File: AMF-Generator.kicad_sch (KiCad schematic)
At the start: 47 parts, among them Q1 ISC012N04LM6ATMA1, Q2 ISC012N04LM6ATMA1, T1 PL300-104L, U1 ACS732KLATR-75AB, U2 UCC21540

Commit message: Basically done with schematic, will split to different PCBs now
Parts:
- C10, C11, C12, C13, C14, C15, C16, C17, C18, C19, C20, C21, C4, C5, C6, C7, C8, C9: footprint (none) -> Capacitor_SMD:C_2220_5650Metric
- C34, C35, C36, C37: footprint (none) -> Capacitor_SMD:C_0805_2012Metric
- R1, R2, R3, R4, R5, R6, R7: footprint (none) -> Resistor_SMD:R_0805_2012Metric
- R10, R8: value 180m -> 1
- R11: value R_Small -> 3.3K
- R12: value R_Small -> 1K
- R9: value 510m -> 1
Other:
- note added: "Double check capacitor ampacity"
- note added: "TODOS: x Bypass Caps x Pullup R values? x Define R11, R12 x Rerun LTSPICE with new gate resistor order x Set I2C ADDR * Double check capacitor ampacity"
- note removed: "TODOS: x Bypass Caps * Pullup R values? * Define R11, R12 * Rerun LTSPICE with new gate resistor order * Set I2C ADDR"
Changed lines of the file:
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@@
     (stroke (width 0) (type default))
+  )
+  (text "Double check capacitor ampacity" (at 214.63 19.05 0)
+    (effects (font (size 1.27 1.27)) (justify left bottom))
   )
   (text "NOTE: FAULT is Open Drain\nNormally pulled to GND" (at 253.365 115.57 0)
@@
     (effects (font (size 1.27 1.27)) (justify left bottom))
   )
-  (text "TODOS:\nx Bypass Caps\n* Pullup R values?\n* Define R11, R12\n* Rerun LTSPICE with new gate resistor order\n* Set I2C ADDR\n"
+  (text "TODOS:\nx Bypass Caps\nx Pullup R values?\nx Define R11, R12\nx Rerun LTSPICE with new gate resistor order\nx Set I2C ADDR\n* Double check capacitor ampacity\n"
     (at 166.37 112.395 0)
     (effects (font (size 1.27 1.27)) (justify left bottom))
@@
       (effects (font (size 1.27 1.27)) (justify left))
     )
-    (property "Footprint" "" (at 49.53 82.55 0)
+    (property "Footprint" "Capacitor_SMD:C_0805_2012Metric" (at 49.53 82.55 0)
       (effects (font (size 1.27 1.27)) hide)
     )
@@
       (effects (font (size 1.27 1.27)))
     )
-    (property "Value" "180m" (at 184.15 57.15 90)
+    (property "Value" "1" (at 184.15 57.15 90)
       (effects (font (size 1.27 1.27)))
     )
@@
       (effects (font (size 1.27 1.27)) (justify left))
     )
-    (property "Footprint" "" (at 96.52 86.36 0)
+    (property "Footprint" "Resistor_SMD:R_0805_2012Metric" (at 96.52 86.36 0)
       (effects (font (size 1.27 1.27)) hide)
     )
@@
       (effects (font (size 1.27 1.27)))
     )
-    (property "Footprint" "" (at 237.49 71.12 0)
+    (property "Footprint" "Capacitor_SMD:C_2220_5650Metric" (at 237.49 71.12 0)
       (effects (font (size 1.27 1.27)) hide)
     )
@@
       (effects (font (size 1.27 1.27)))
     )
-    (property "Footprint" "" (at 237.49 26.67 0)
+    (property "Footprint" "Capacitor_SMD:C_2220_5650Metric" (at 237.49 26.67 0)
       (effects (font (size 1.27 1.27)) hide)
     )
@@
       (effects (font (size 1.27 1.27)))
     )
-    (property "Footprint" "" (at 228.6 62.23 0)
+    (property "Footprint" "Capacitor_SMD:C_2220_5650Metric" (at 228.6 62.23 0)
       (effects (font (size 1.27 1.27)) hide)
     )
@@
       (effects (font (size 1.27 1.27)) (justify left))
     )
-    (property "Footprint" "" (at 143.51 80.01 0)
+    (property "Footprint" "Resistor_SMD:R_0805_2012Metric" (at 143.51 80.01 0)
       (effects (font (size 1.27 1.27)) hide)
     )
@@
       (effects (font (size 1.27 1.27)))
     )
-    (property "Footprint" "" (at 119.38 97.79 0)
+    (property "Footprint" "Resistor_SMD:R_0805_2012Metric" (at 119.38 97.79 0)
       (effects (font (size 1.27 1.27)) hide)
     )
@@
       (effects (font (size 1.27 1.27)))
     )
-    (property "Footprint" "" (at 92.71 82.55 0)
+    (property "Footprint" "Resistor_SMD:R_0805_2012Metric" (at 92.71 82.55 0)
       (effects (font (size 1.27 1.27)) hide)
     )
@@
       (effects (font (size 1.27 1.27)))
     )
-    (property "Footprint" "" (at 219.71 26.67 0)
+    (property "Footprint" "Capacitor_SMD:C_2220_5650Metric" (at 219.71 26.67 0)
       (effects (font (size 1.27 1.27)) hide)
     )
@@
       (effects (font (size 1.27 1.27)))
     )
-    (property "Value" "510m" (at 184.15 66.04 90)
+    (property "Value" "1" (at 184.15 66.04 90)
       (effects (font (size 1.27 1.27)))
     )
@@
       (effects (font (size 1.27 1.27)))
     )
-    (property "Value" "180m" (at 184.15 74.93 90)
+    (property "Value" "1" (at 184.15 74.93 90)
       (effects (font (size 1.27 1.27)))
     )
@@
       (effects (font (size 1.27 1.27)))
     )
-    (property "Footprint" "" (at 219.71 35.56 0)
+    (property "Footprint" "Capacitor_SMD:C_2220_5650Metric" (at 219.71 35.56 0)
       (effects (font (size 1.27 1.27)) hide)
     )
@@
       (effects (font (size 1.27 1.27)))
     )
-    (property "Footprint" "" (at 219.71 62.23 0)
+    (property "Footprint" "Capacitor_SMD:C_2220_5650Metric" (at 219.71 62.23 0)
       (effects (font (size 1.27 1.27)) hide)
     )
@@
       (effects (font (size 1.27 1.27)))
     )
-    (property "Footprint" "" (at 219.71 71.12 0)
+    (property "Footprint" "Capacitor_SMD:C_2220_5650Metric" (at 219.71 71.12 0)
       (effects (font (size 1.27 1.27)) hide)
     )
@@
       (effects (font (size 1.27 1.27)) (justify left))
     )
-    (property "Footprint" "" (at 116.84 62.23 0)
+    (property "Footprint" "Resistor_SMD:R_0805_2012Metric" (at 116.84 62.23 0)
       (effects (font (size 1.27 1.27)) hide)
     )
@@
       (effects (font (size 1.27 1.27)))
     )
-    (property "Footprint" "" (at 219.71 44.45 0)
+    (property "Footprint" "Capacitor_SMD:C_2220_5650Metric" (at 219.71 44.45 0)
       (effects (font (size 1.27 1.27)) hide)
     )
@@
       (effects (font (size 1.27 1.27)))
     )
-    (property "Footprint" "" (at 228.6 44.45 0)
+    (property "Footprint" "Capacitor_SMD:C_2220_5650Metric" (at 228.6 44.45 0)
       (effects (font (size 1.27 1.27)) hide)
     )
@@
       (effects (font (size 1.27 1.27)))
     )
-    (property "Value" "R_Small" (at 227.965 100.33 90)
+    (property "Value" "1K" (at 227.965 100.33 90)
       (effects (font (size 1.27 1.27)))
     )
@@
       (effects (font (size 1.27 1.27)) (justify left))
     )
-    (property "Footprint" "" (at 92.075 109.22 0)
+    (property "Footprint" "Capacitor_SMD:C_0805_2012Metric" (at 92.075 109.22 0)
       (effects (font (size 1.27 1.27)) hide)
     )
@@
       (effects (font (size 1.27 1.27)) (justify left))
     )
-    (property "Footprint" "" (at 89.535 67.945 0)
+    (property "Footprint" "Capacitor_SMD:C_0805_2012Metric" (at 89.535 67.945 0)
       (effects (font (size 1.27 1.27)) hide)
     )
@@
       (effects (font (size 1.27 1.27)) (justify left))
     )
-    (property "Footprint" "" (at 255.905 88.265 0)
+    (property "Footprint" "Capacitor_SMD:C_0805_2012Metric" (at 255.905 88.265 0)
       (effects (font (size 1.27 1.27)) hide)
     )
@@
       (effects (font (size 1.27 1.27)))
     )
-    (property "Footprint" "" (at 228.6 26.67 0)
+    (property "Footprint" "Capacitor_SMD:C_2220_5650Metric" (at 228.6 26.67 0)
       (effects (font (size 1.27 1.27)) hide)
     )
@@
   (symbol (lib_id "Device:R_Small") (at 233.045 95.25 0) (unit 1)
     (in_bom yes) (on_board yes) (dnp no) (fields_autoplaced)
-    (property "Reference" "R11" (at 235.585 94.615 0)
-      (effects (font (size 1.27 1.27)) (justify left))
-    )
-    (property "Value" "R_Small" (at 235.585 97.155 0)
+    (property "Reference" "R11" (at 234.95 94.615 0)
+      (effects (font (size 1.27 1.27)) (justify left))
+    )
+    (property "Value" "3.3K" (at 234.95 97.155 0)
       (effects (font (size 1.27 1.27)) (justify left))
     )
@@
       (effects (font (size 1.27 1.27)) (justify left))
     )
-    (property "Footprint" "" (at 52.07 101.6 0)
+    (property "Footprint" "Resistor_SMD:R_0805_2012Metric" (at 52.07 101.6 0)
       (effects (font (size 1.27 1.27)) hide)
     )
@@
       (effects (font (size 1.27 1.27)))
     )
-    (property "Footprint" "" (at 237.49 53.34 0)
+    (property "Footprint" "Capacitor_SMD:C_2220_5650Metric" (at 237.49 53.34 0)
       (effects (font (size 1.27 1.27)) hide)
     )
@@
       (effects (font (size 1.27 1.27)))
     )
-    (property "Footprint" "" (at 237.49 62.23 0)
+    (property "Footprint" "Capacitor_SMD:C_2220_5650Metric" (at 237.49 62.23 0)
       (effects (font (size 1.27 1.27)) hide)
     )
@@
       (effects (font (size 1.27 1.27)))
     )
-    (property "Footprint" "" (at 228.6 71.12 0)
+    (property "Footprint" "Capacitor_SMD:C_2220_5650Metric" (at 228.6 71.12 0)
       (effects (font (size 1.27 1.27)) hide)
     )
@@
       (effects (font (size 1.27 1.27)))
     )
-    (property "Footprint" "" (at 237.49 35.56 0)
+    (property "Footprint" "Capacitor_SMD:C_2220_5650Metric" (at 237.49 35.56 0)
       (effects (font (size 1.27 1.27)) hide)
     )
@@
       (effects (font (size 1.27 1.27)))
     )
-    (property "Footprint" "" (at 228.6 53.34 0)
+    (property "Footprint" "Capacitor_SMD:C_2220_5650Metric" (at 228.6 53.34 0)
       (effects (font (size 1.27 1.27)) hide)
     )
@@
       (effects (font (size 1.27 1.27)) (justify left))
     )
-    (property "Footprint" "" (at 123.19 101.6 0)
+    (property "Footprint" "Resistor_SMD:R_0805_2012Metric" (at 123.19 101.6 0)
       (effects (font (size 1.27 1.27)) hide)
     )
@@
       (effects (font (size 1.27 1.27)))
     )
-    (property "Footprint" "" (at 219.71 53.34 0)
+    (property "Footprint" "Capacitor_SMD:C_2220_5650Metric" (at 219.71 53.34 0)
       (effects (font (size 1.27 1.27)) hide)
     )
@@
       (effects (font (size 1.27 1.27)))
     )
-    (property "Footprint" "" (at 228.6 35.56 0)
+    (property "Footprint" "Capacitor_SMD:C_2220_5650Metric" (at 228.6 35.56 0)
       (effects (font (size 1.27 1.27)) hide)
     )
@@
       (effects (font (size 1.27 1.27)))
     )
-    (property "Footprint" "" (at 237.49 44.45 0)
-      (effects (font (size 1.27 1.27)) hide)
-    )
+    (property "Footprint" "Capacitor_SMD:C_2220_5650Metric" (at 237.49 44.45 0)
+      (effects (font (size 1.27 1.27)) hide)
+    )

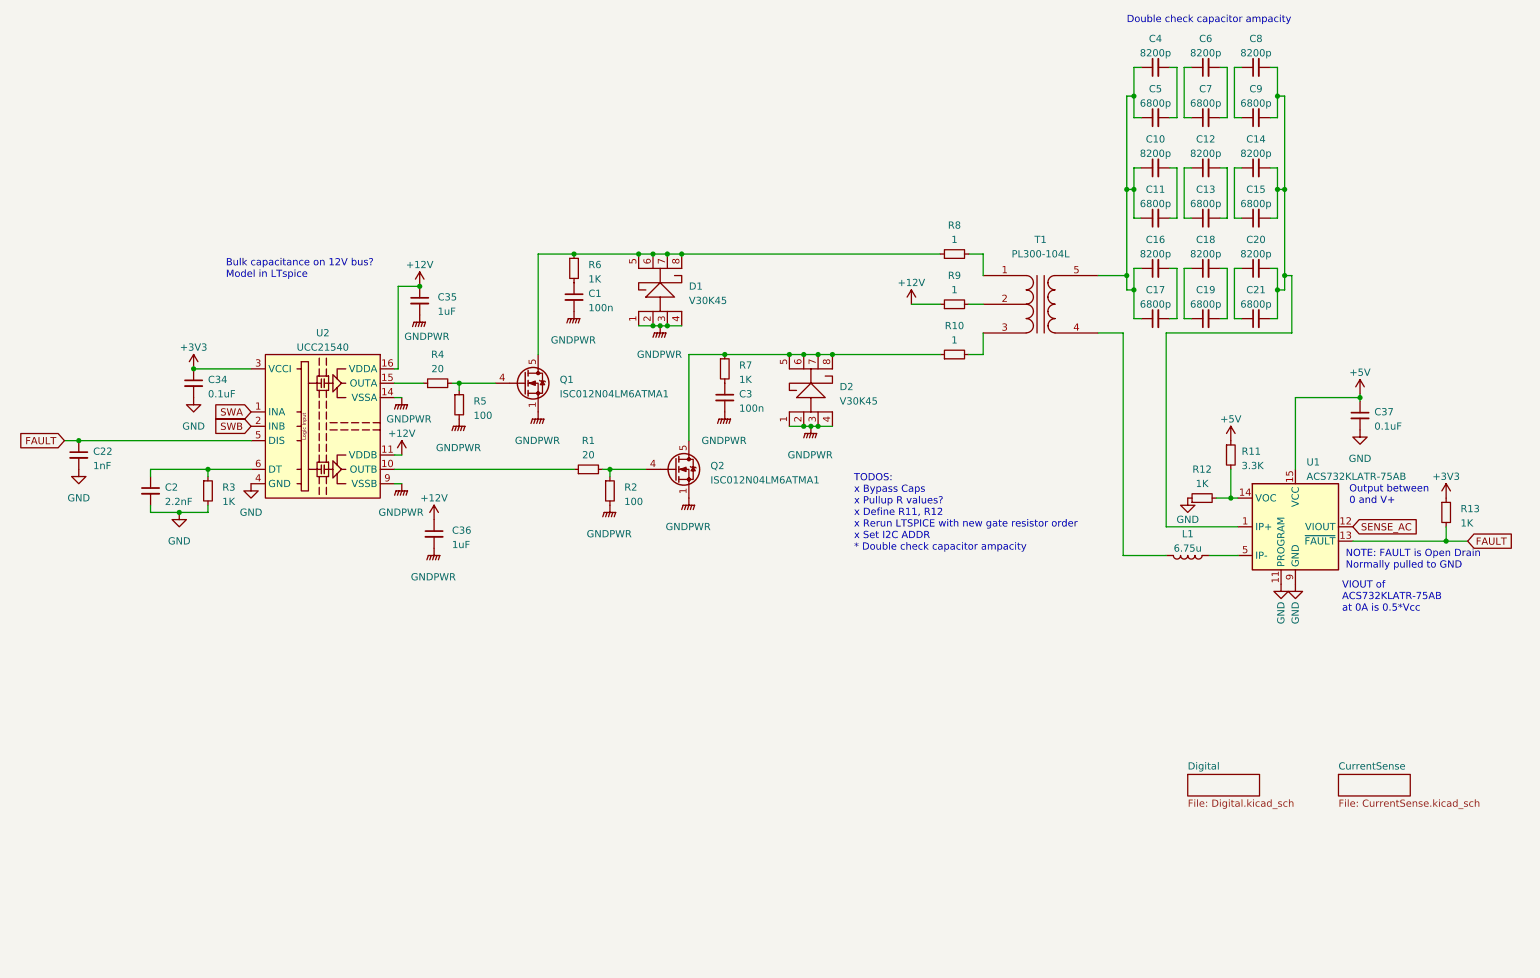
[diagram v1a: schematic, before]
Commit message: Finished footprint assignment
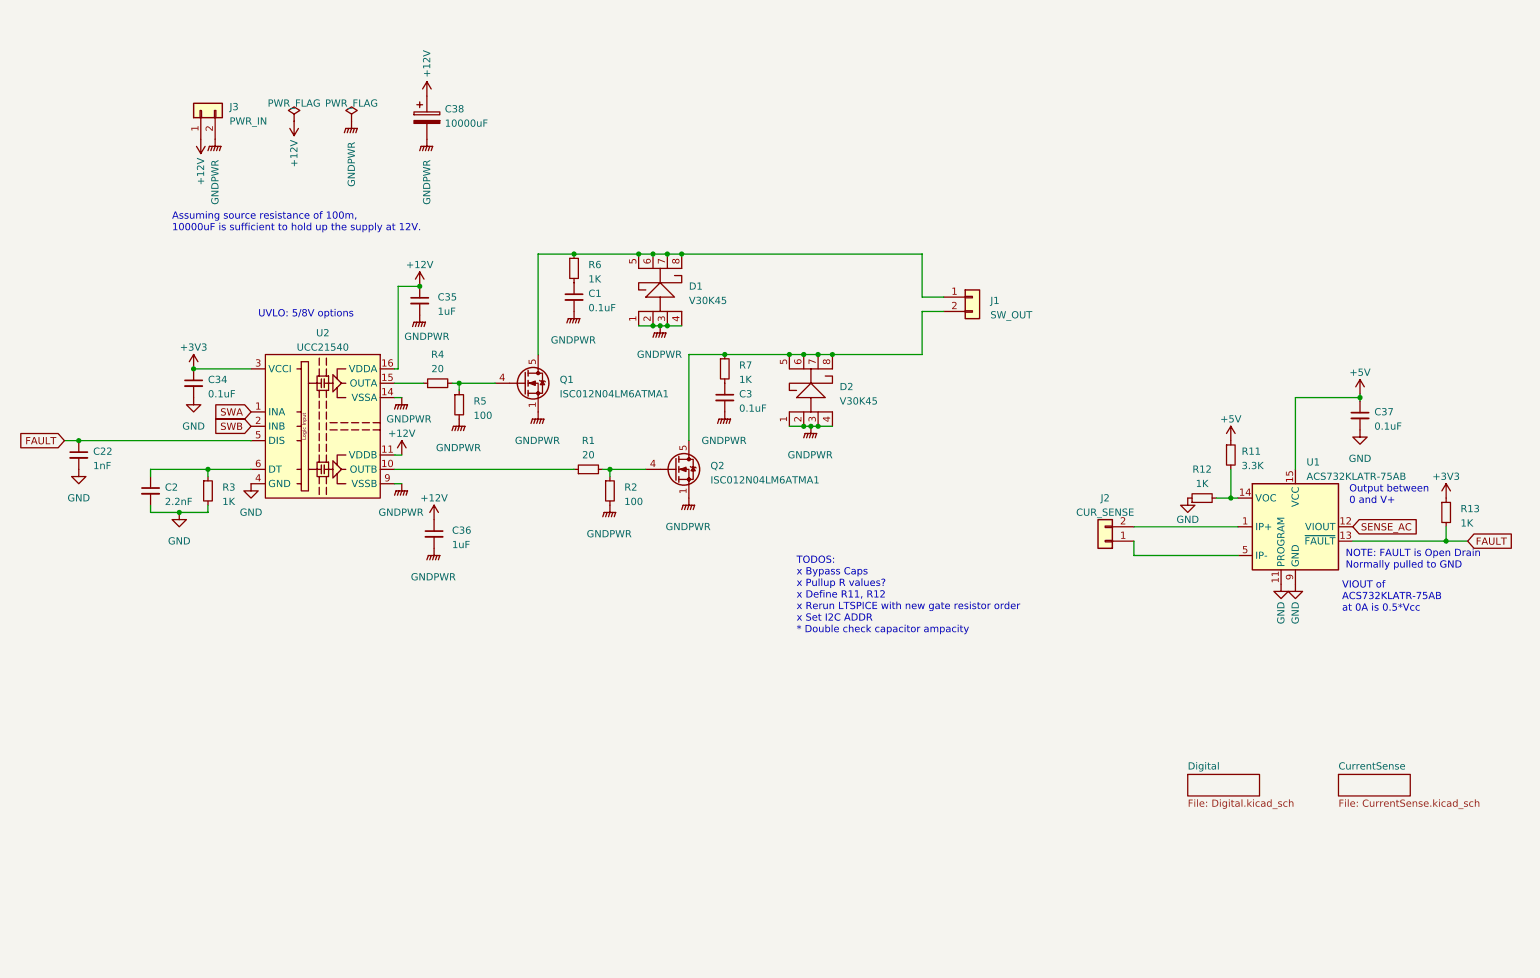
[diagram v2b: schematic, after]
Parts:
- removed C10, C12, C14, C16, C18, C20, C4, C6, C8: 8200p, Capacitor_SMD:C_2220_5650Metric, symbol Device:C_Small
- removed C11, C13, C15, C17, C19, C21, C5, C7, C9: 6800p, Capacitor_SMD:C_2220_5650Metric, symbol Device:C_Small
- removed L1: 6.75u, symbol Device:L
- removed R10, R8, R9: 1, symbol Device:R_Small
- removed T1: PL300-104L, symbol Device:Transformer_SP_1S
- added C38: 10000uF, Capacitor_THT:CP_Radial_D22.0mm_P10.00mm_SnapIn, symbol Device:C_Polarized
- added J1: SW_OUT, 8PCV-02-006:8PCV02006, symbol Connector_Generic:Conn_01x02
- added J2: CUR_SENSE, 8PCV-02-006:8PCV02006, symbol Connector_Generic:Conn_01x02
- added J3: PWR_IN, 8PCV-02-006:8PCV02006, symbol Connector_Generic:Conn_01x02
- C1, C3: value 100n -> 0.1uF; footprint (none) -> Capacitor_SMD:C_0805_2012Metric
- C2, C22: footprint (none) -> Capacitor_SMD:C_0805_2012Metric
- R11, R12, R13: footprint (none) -> Resistor_SMD:R_0805_2012Metric
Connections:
- net +12V: now also C38.1, J3.1 (Pin_1)
- net GNDPWR: now also C38.2, J3.2 (Pin_2)
- net at D1.5, D1.6, D1.7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: now also J1.1 (Pin_1)
- net at U1.1 (IP+), U1.2 (IP+), U1.3 (IP+)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: now also J2.2 (Pin_2)
- net at D2.5, D2.6, D2.7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: now also J1.2 (Pin_2)
- net at U1.5 (IP-), U1.6 (IP-), U1.7 (IP-)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: now also J2.1 (Pin_1)
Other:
- note added: "Assuming source resistance of 100m, 10000uF is sufficient to hold up the supply at 12V."
- note added: "UVLO: 5/8V options"
- note removed: "Bulk capacitance on 12V bus? Model in LTspice"
- note removed: "Double check capacitor ampacity"

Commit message: Added a couple notes
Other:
- note added: "TODOS: x Bypass Caps x Pullup R values? x Define R11, R12 x Rerun LTSPICE with new gate resistor order x Set I2C ADDR * Double check capacitor ampacity * Double check FAULT logic"
- note added: "VOC: 0.25*Vcc"
- note removed: "TODOS: x Bypass Caps x Pullup R values? x Define R11, R12 x Rerun LTSPICE with new gate resistor order x Set I2C ADDR * Double check capacitor ampacity"
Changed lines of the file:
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@@
     (effects (font (size 1.27 1.27)) (justify left bottom))
   )
-  (text "TODOS:\nx Bypass Caps\nx Pullup R values?\nx Define R11, R12\nx Rerun LTSPICE with new gate resistor order\nx Set I2C ADDR\n* Double check capacitor ampacity\n"
+  (text "VOC: 0.25*Vcc" (at 216.535 95.885 0)
+    (effects (font (size 1.27 1.27)) (justify left bottom))
+  )
+  (text "TODOS:\nx Bypass Caps\nx Pullup R values?\nx Define R11, R12\nx Rerun LTSPICE with new gate resistor order\nx Set I2C ADDR\n* Double check capacitor ampacity\n* Double check FAULT logic"
     (at 156.21 127 0)
     (effects (font (size 1.27 1.27)) (justify left bottom))

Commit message: Initial pass of component placement complete. Added test points and i2c headers, also changed 12V input to terminal block
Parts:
- removed C38: 10000uF, Capacitor_THT:CP_Radial_D22.0mm_P10.00mm_SnapIn, symbol Device:C_Polarized
- J3: footprint 8PCV-02-006:8PCV02006 -> TerminalBlock:TerminalBlock_bornier-2_P5.08mm
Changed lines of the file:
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@@
       (effects (font (size 1.27 1.27)) (justify right))
     )
-    (property "Footprint" "8PCV-02-006:8PCV02006" (at 50.8 34.29 0)
+    (property "Footprint" "TerminalBlock:TerminalBlock_bornier-2_P5.08mm" (at 50.8 34.29 0)
       (effects (font (size 1.27 1.27)) hide)
     )
@@
         (path "/c3df021c-646c-4a68-ac14-a081c2121d02"
           (reference "#PWR062") (unit 1)
-        )
-      )
-    )
-  )
-  (symbol (lib_id "power:+12V") (at 90.805 31.75 0) (unit 1)
-    (in_bom yes) (on_board yes) (dnp no)
-    (property "Reference" "#PWR060" (at 90.805 35.56 0)
-      (effects (font (size 1.27 1.27)) hide)
-    )
-    (property "Value" "+12V" (at 90.805 26.035 90)
-      (effects (font (size 1.27 1.27)))
-    )
-    (property "Footprint" "" (at 90.805 31.75 0)
-      (effects (font (size 1.27 1.27)) hide)
-    )
-    (property "Datasheet" "" (at 90.805 31.75 0)
-      (effects (font (size 1.27 1.27)) hide)
-    )
-    (pin "1")
-    (instances
-      (project "AMF-Generator"
-        (path "/c3df021c-646c-4a68-ac14-a081c2121d02"
-          (reference "#PWR060") (unit 1)
         )
       )
@@
     )
   )
-  (symbol (lib_id "power:GNDPWR") (at 90.805 39.37 0) (unit 1)
-    (in_bom yes) (on_board yes) (dnp no)
-    (property "Reference" "#PWR061" (at 90.805 44.45 0)
-      (effects (font (size 1.27 1.27)) hide)
-    )
-    (property "Value" "GNDPWR" (at 90.805 46.99 90)
-      (effects (font (size 1.27 1.27)))
-    )
-    (property "Footprint" "" (at 90.805 40.64 0)
-      (effects (font (size 1.27 1.27)) hide)
-    )
-    (property "Datasheet" "" (at 90.805 40.64 0)
-      (effects (font (size 1.27 1.27)) hide)
-    )
-    (pin "1")
-    (instances
-      (project "AMF-Generator"
-        (path "/c3df021c-646c-4a68-ac14-a081c2121d02"
-          (reference "#PWR061") (unit 1)
-        )
-      )
-    )
-  )
   (symbol (lib_id "power:+12V") (at 86.36 95.25 0) (unit 1)
     (in_bom yes) (on_board yes) (dnp no) (fields_autoplaced)
@@
         )
       )
-    )
-  )
-  (symbol (lib_id "Device:C_Polarized") (at 90.805 35.56 0) (unit 1)
-    (in_bom yes) (on_board yes) (dnp no) (fields_autoplaced)
-    (property "Reference" "C38" (at 93.98 34.036 0)
-      (effects (font (size 1.27 1.27)) (justify left))
-    )
-    (property "Value" "10000uF" (at 93.98 36.576 0)
-      (effects (font (size 1.27 1.27)) (justify left))
-    )
-    (property "Footprint" "Capacitor_THT:CP_Radial_D22.0mm_P10.00mm_SnapIn" (at 91.7702 39.37 0)
-      (effects (font (size 1.27 1.27)) hide)
-    )
-    (property "Datasheet" "~" (at 90.805 35.56 0)
-      (effects (font (size 1.27 1.27)) hide)
-    )
-    (pin "1")
-    (pin "2")
-    (instances
-      (project "AMF-Generator"
-        (path "/c3df021c-646c-4a68-ac14-a081c2121d02"
-          (reference "C38") (unit 1)
-        )
-      )
